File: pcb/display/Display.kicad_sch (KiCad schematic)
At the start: 33 parts, among them J1 Screw_Terminal_01x04, J2 RJ45, J4 Conn_01x08_Pin, P1 USB_C_Plug_USB2.0, SW1 SW_Push, SW2 SW_Push, SW3 SW_Push, SW4 SW_Push, U1 TMP1075DSG, U2 ESP32-S3-MINI-1

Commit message: Final Version of Prototype Rev. 00
Switched back to PCA9685 for PWM, removed high side switch
Updated some component values
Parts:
- C10, C11: value 100n -> 10p; now not fitted
- J1: value Screw_Terminal_01x04 -> Screw Terminal 3.5mm
- J4: value Conn_01x08_Pin -> 01x08_Pin
- R17, R43: value 20k -> 1k
- R46, R47: value 20k -> 4k3
- R8, R9: value 1k -> 0R
- SW1, SW2, SW3, SW4: value SW_Push -> SW_4x3mm
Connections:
- net PWM.OE: now reaches U2.27 (GPIO47/SPICLK_P/SUBSPICLK_P_DIFF)
- net BRIGHTNESS: no longer names the net of U2.26 (GPIO26)
- no-connect marks 13 -> 14
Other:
- sheet Communication ports: added none; removed VIN+, VIN-
- sheet LED Driver ports: added PWM_OE; removed DIM_PWM
- sheet Power Supply ports: added none; removed 12V_PG
- moved on the sheet: C2, C27, C3, C4, D24, D25, J4, R15, R17, R43, R46, R47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

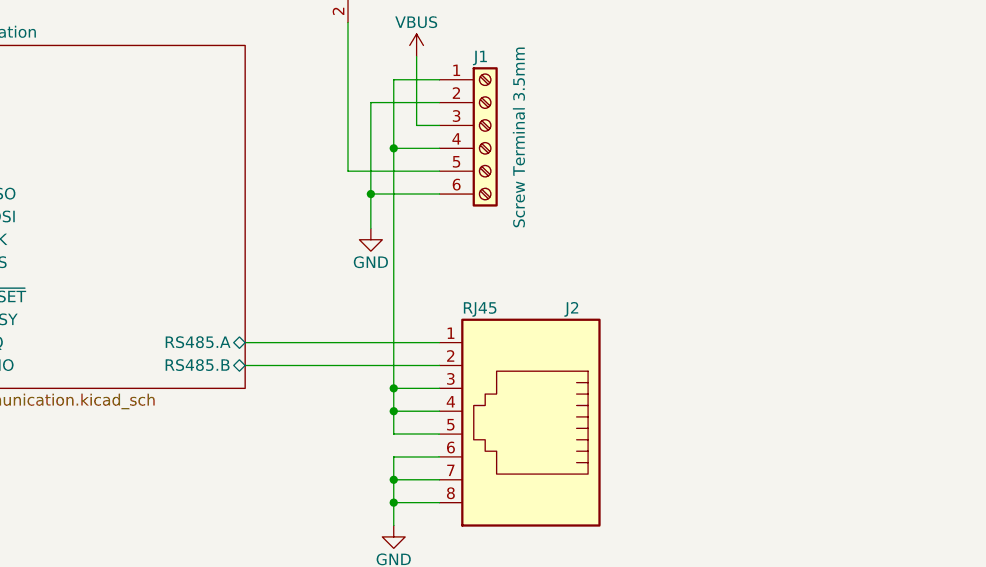
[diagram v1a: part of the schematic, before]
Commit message: Marked known issues in schematic
Add gitignore
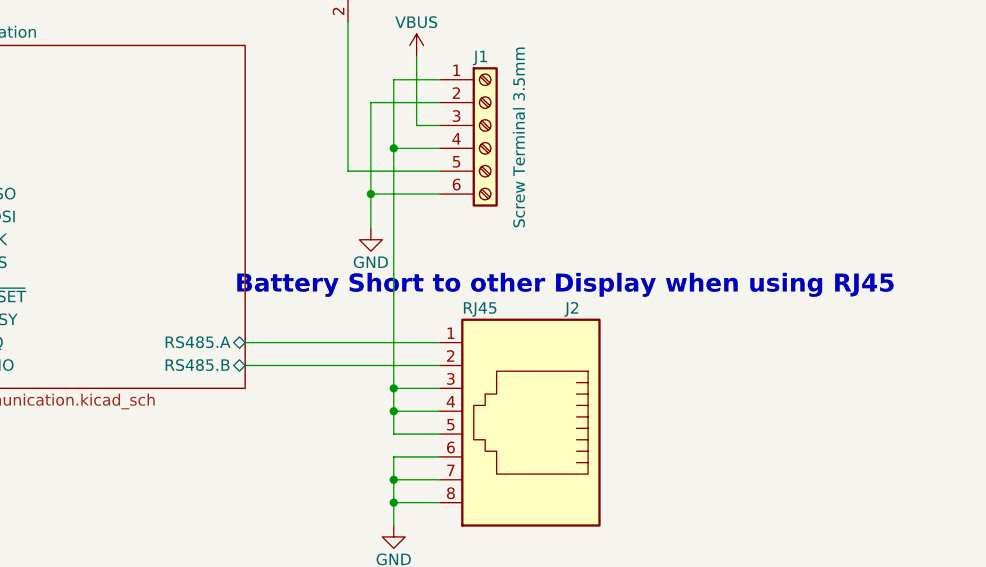
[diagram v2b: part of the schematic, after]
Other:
- note added: "Battery Short to other Display when using RJ45"
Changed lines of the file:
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@@
+		)
+	)
+	(text "Battery Short to other Display when using RJ45"
+		(exclude_from_sim no)
+		(at 276.86 57.15 0)
+		(effects
+			(font
+				(size 2 2)
+				(thickness 0.4)
+				(bold yes)
+				(color 255 153 0 1)
+			)
 		)
 	)

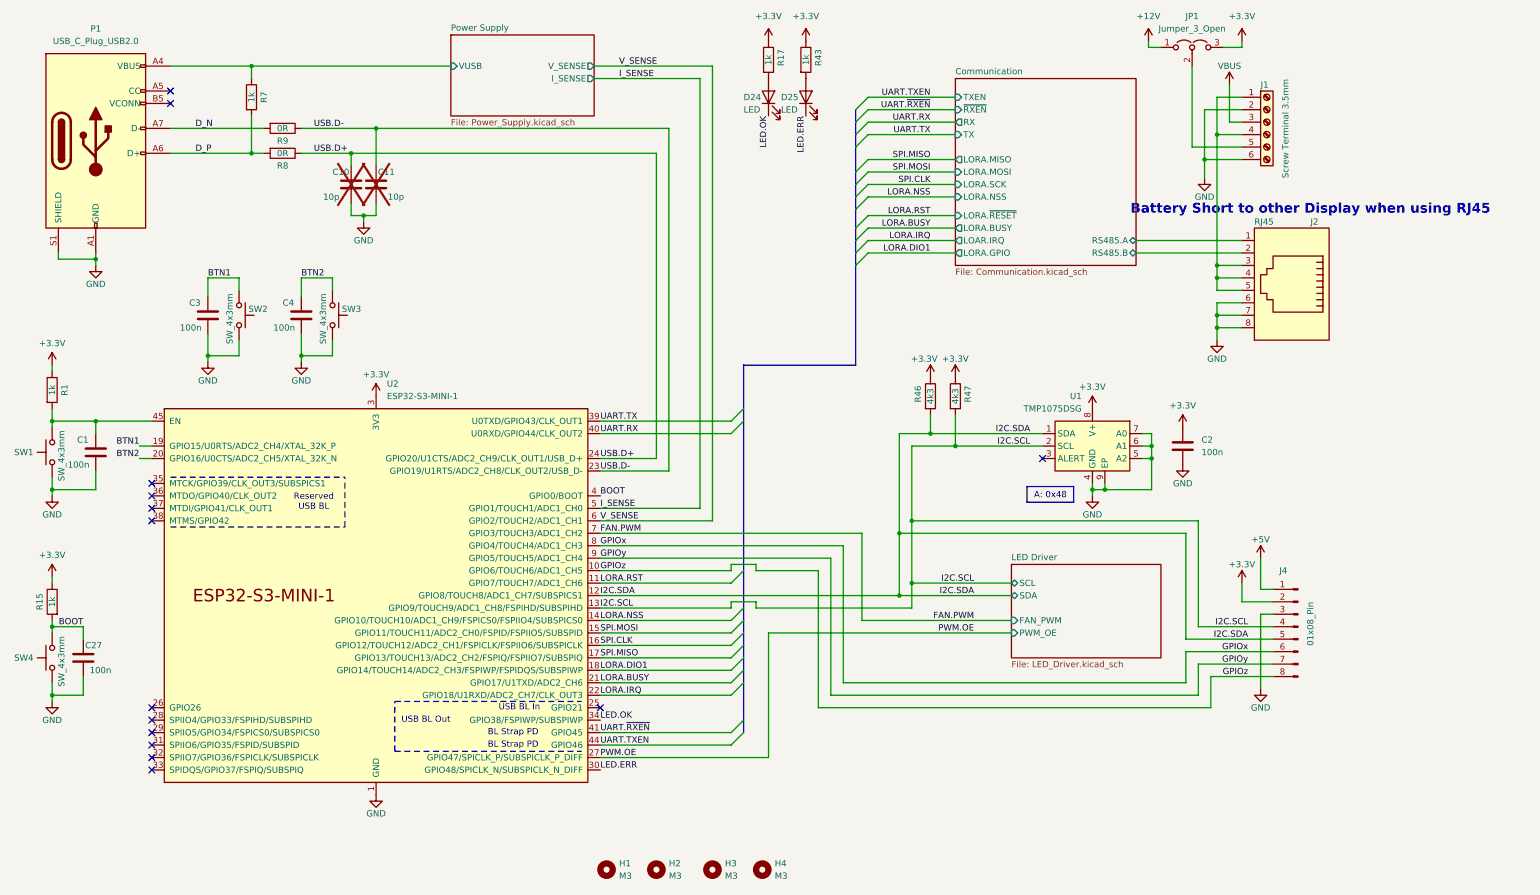
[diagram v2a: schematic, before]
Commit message: Display HW Revision 01
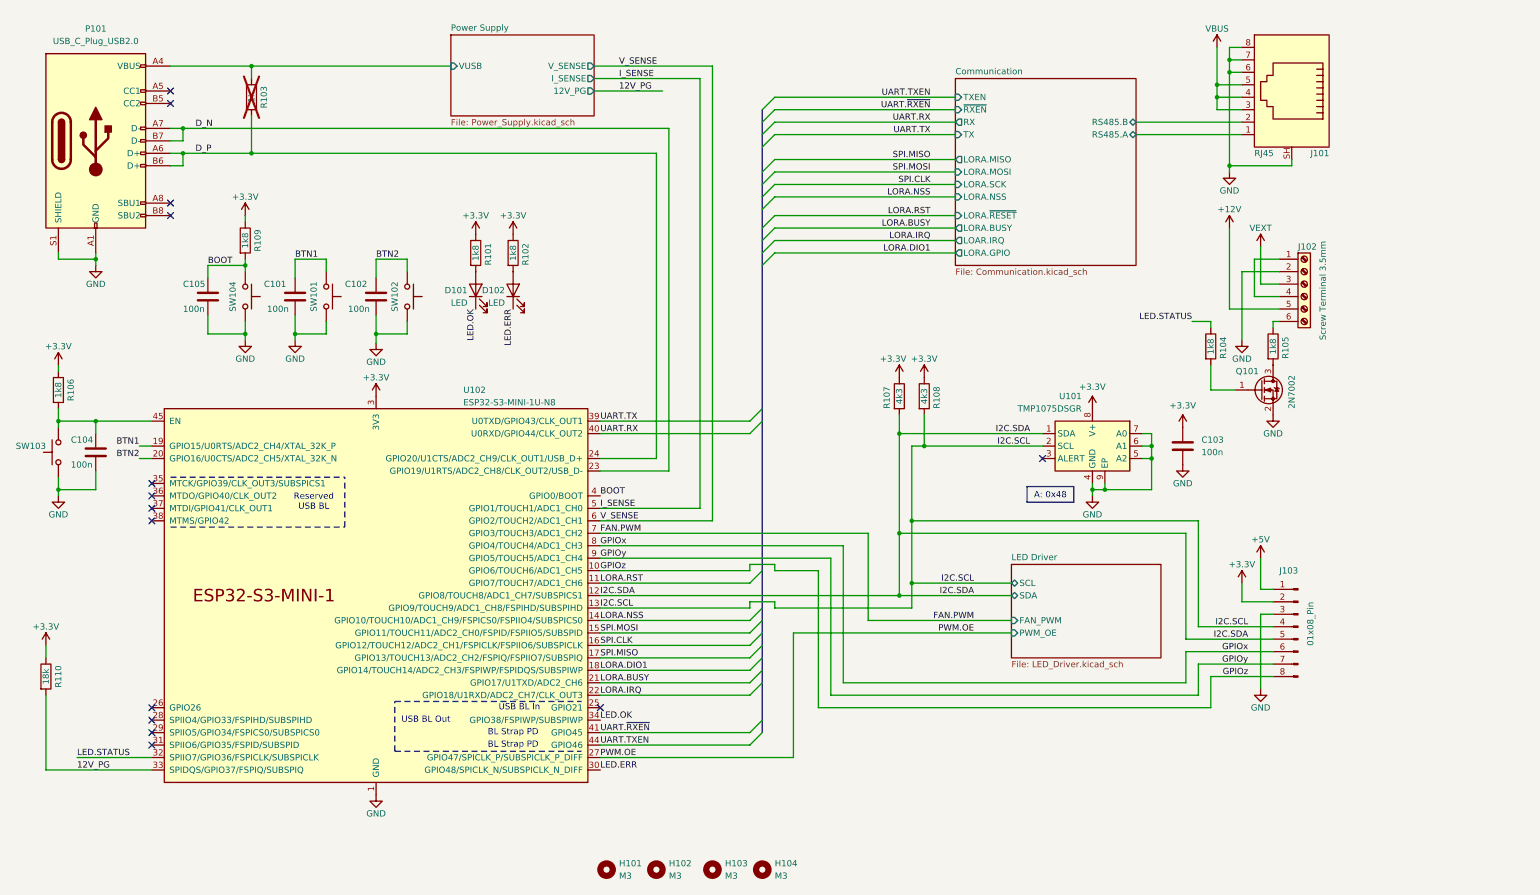
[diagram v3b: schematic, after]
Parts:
- removed C10, C11: 10p, Resistor_SMD:R_0402_1005Metric, symbol Device:C
- removed JP1: Jumper_3_Open, Connector_PinHeader_2.54mm:PinHeader_1x03_P2.54mm_Vertical, symbol Jumper:Jumper_3_Open
- removed R8, R9: 0R, Resistor_SMD:R_0402_1005Metric, symbol Device:R
- added Q101: 2N7002, Package_TO_SOT_SMD:SOT-23, symbol Transistor_FET:2N7002
- added R104, R105: 1k8, Resistor_SMD:R_0402_1005Metric, symbol Device:R
- added R110: 18k, Resistor_SMD:R_0402_1005Metric, symbol Device:R
- C101: renamed from C3; footprint Capacitor_SMD:C_0603_1608Metric -> Capacitor_SMD:C_0402_1005Metric; JLC PN (none) -> C307331
- C102: renamed from C4; footprint Capacitor_SMD:C_0603_1608Metric -> Capacitor_SMD:C_0402_1005Metric; JLC PN (none) -> C307331
- C103: renamed from C2; footprint Capacitor_SMD:C_0603_1608Metric -> Capacitor_SMD:C_0402_1005Metric; JLC PN (none) -> C307331
- C104: renamed from C1; footprint Capacitor_SMD:C_0603_1608Metric -> Capacitor_SMD:C_0402_1005Metric; JLC PN (none) -> C307331
- C105: renamed from C27; footprint Capacitor_SMD:C_0603_1608Metric -> Capacitor_SMD:C_0402_1005Metric; JLC PN (none) -> C307331
- D101: renamed from D24; JLC PN (none) -> C2286
- D102: renamed from D25; JLC PN (none) -> C2286
- J101: renamed from J2; footprint Connector_RJ:RJ45_Amphenol_54602-x08_Horizontal -> Connector_RJ:RJ45_Amphenol_RJHSE5380; symbol Connector:RJ45 -> Connector:RJ45_Shielded; JLC PN (none) -> C19078599
- J102: renamed from J1; JLC PN (none) -> C409119
- P101: renamed from P1; symbol Connector:USB_C_Plug_USB2.0 -> Connector:USB_C_Receptacle_USB2.0_16P; JLC PN (none) -> C2927039
- R101: renamed from R17; value 1k -> 1k8; footprint Resistor_SMD:R_0603_1608Metric -> Resistor_SMD:R_0402_1005Metric
- R102: renamed from R43; value 1k -> 1k8; footprint Resistor_SMD:R_0603_1608Metric -> Resistor_SMD:R_0402_1005Metric
- R103: renamed from R7; footprint Resistor_SMD:R_0603_1608Metric -> Resistor_SMD:R_0402_1005Metric; now not fitted
- R106: renamed from R1; value 1k -> 1k8; footprint Resistor_SMD:R_0603_1608Metric -> Resistor_SMD:R_0402_1005Metric
- R107: renamed from R46; footprint Resistor_SMD:R_0603_1608Metric -> Resistor_SMD:R_0402_1005Metric
- R108: renamed from R47; footprint Resistor_SMD:R_0603_1608Metric -> Resistor_SMD:R_0402_1005Metric
- R109: renamed from R15; value 1k -> 1k8; footprint Resistor_SMD:R_0603_1608Metric -> Resistor_SMD:R_0402_1005Metric
- SW101: renamed from SW2; JLC PN (none) -> C18078117
- SW102: renamed from SW3; JLC PN (none) -> C18078117
- SW103: renamed from SW1; JLC PN (none) -> C18078117
- SW104: renamed from SW4; JLC PN (none) -> C18078117
- U101: renamed from U1; value TMP1075DSG -> TMP1075DSGR; JLC PN (none) -> C2870250
- U102: renamed from U2; value ESP32-S3-MINI-1 -> ESP32-S3-MINI-1U-N8; JLC PN (none) -> C2980299
- renumbered H1 to H101, H2 to H102, H3 to H103, H4 to H104, J4 to J103
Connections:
- net USB.D+ is gone; now on net D_P: U102.24 (GPIO20/U1CTS/ADC2_CH9/CLK_OUT1/USB_D+)
- net USB.D- is gone; now on net D_N: U102.23 (GPIO19/U1RTS/ADC2_CH8/CLK_OUT2/USB_D-)
- net +12V: now also J102.5 (Pin_5)
- net +3.3V: now also R110.1
- net D_N: now also P101.B7 (D-)
- net D_P: now also P101.B6 (D+)
- net GND: now also J101.SH, Q101.2 (S); no longer J102.6 (Pin_6)
- net VBUS: now also J101.3, J101.4, J101.5; no longer J102.3 (Pin_3)
- net LED.STATUS: now reaches U102.32 (SPIIO7/GPIO36/FSPICLK/SUBSPICLK)
- net LED.STATUS: now also R104.1
- net 12V_PG: now reaches U102.33 (SPIDQS/GPIO37/FSPIQ/SUBSPIQ)
- net 12V_PG: now also R110.2
- new net: J102.6 (Pin_6), R105.1
- new net: Q101.3 (D), R105.2
- new net: Q101.1 (G), R104.2
- new net: J102.1 (Pin_1), J102.4 (Pin_4)
- new net VEXT: J102.3 (Pin_3)
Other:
- sheet Power Supply ports: added 12V_PG; removed none
- note removed: "Battery Short to other Display when using RJ45"
- title: Open-Shot-Clock -> Open Shot Clock - Display
- moved on the sheet: C101, C102, C105, D101, D102, J102, R101, R102, R106, R107, R108, R109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
